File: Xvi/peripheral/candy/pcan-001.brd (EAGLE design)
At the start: 72 x 72 mm, 24 parts

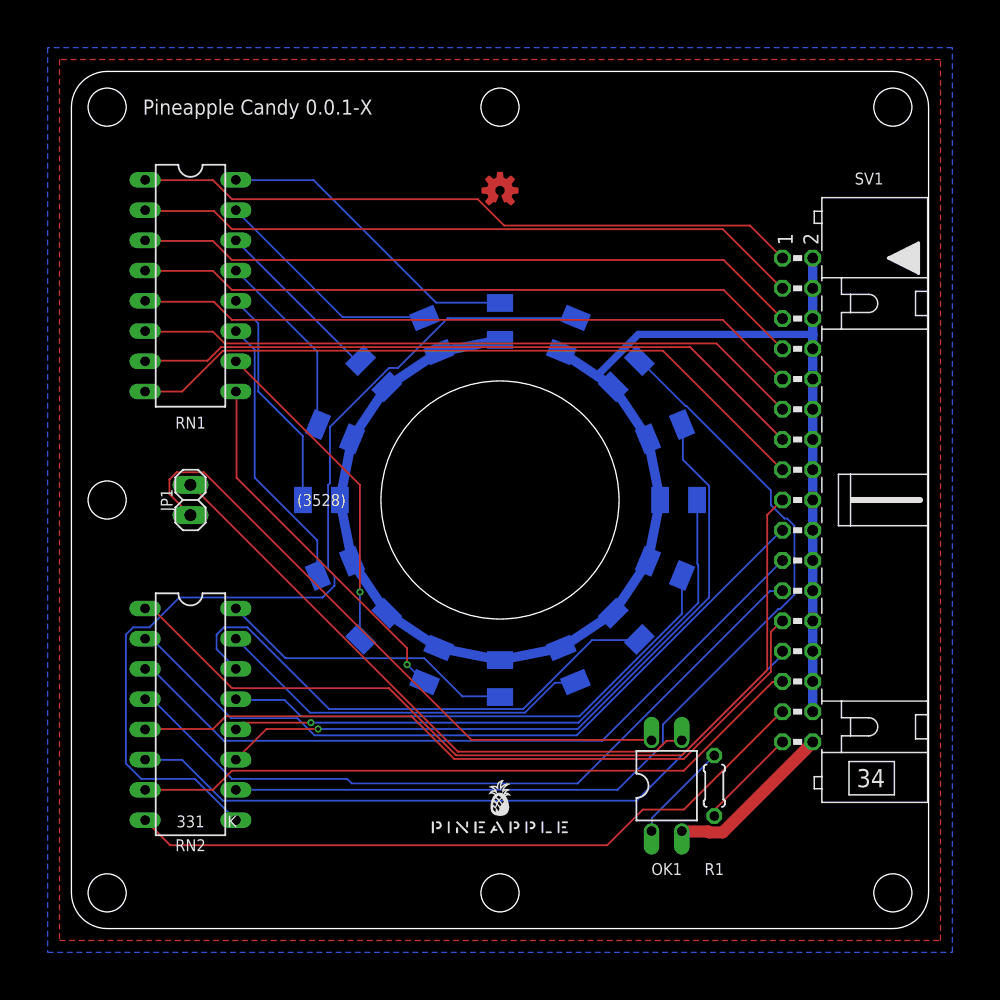
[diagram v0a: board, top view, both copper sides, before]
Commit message: Dual LEDs.
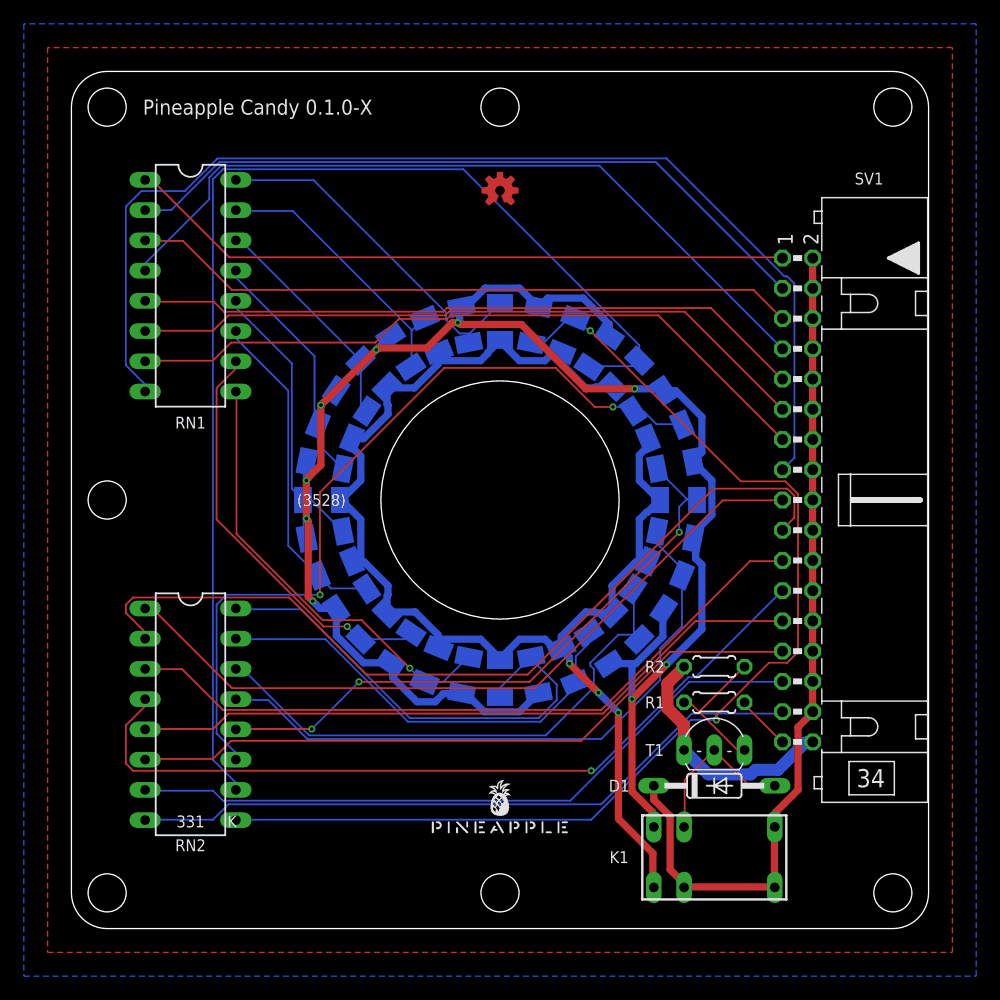
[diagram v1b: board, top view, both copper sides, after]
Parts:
- removed JP1: Optorelay, pinhead:1X02
- removed OK1: LTV816, optocoupler:DIL04
- added D1: 1N4446, diode:DO35-10
- added K1: G5V1, relay:G5V1
- added L17, L18, L19, L20, L21, L22, L23, L24, L25, L26, L27, L28, L29, L30, L31, L32: LP-T35XW-80-BJ, led:KA-3528ASYC
- added R2: (no value), rcl:0204/5
- added T1: 2SC1815, transistor:TO92-ECB
- R1: value 220 -> (none)
- moved R1 7.00 mm to (54.0, 19.0), turned to 0 degrees
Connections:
- removed net N$1: L01.C, RN1.16
- removed net N$10: L10.C, RN2.15
- removed net N$11: L11.C, RN2.14
- removed net N$12: L12.C, RN2.13
- removed net N$13: L13.C, RN2.12
- removed net N$14: L14.C, RN2.11
- removed net N$15: L15.C, RN2.10
- removed net N$16: L16.C, RN2.9
- removed net N$2: L02.C, RN1.15
- removed net N$20: JP1.1, OK1.4
- removed net N$3: L03.C, RN1.14
- removed net N$4: L04.C, RN1.13
- removed net N$5: L05.C, RN1.12
- removed net N$6: L06.C, RN1.11
- removed net N$7: L07.C, RN1.10
- removed net N$8: L08.C, RN1.9
- removed net N$9: L09.C, RN2.16
- new net LD00K: L01.C, L17.C, RN1.16
- new net LD01K: L02.C, L18.C, RN1.15
- new net LD02K: L03.C, L19.C, RN1.14
- new net LD03K: L04.C, L20.C, RN1.13
- new net LD04K: L05.C, L21.C, RN1.12
- new net LD05K: L06.C, L22.C, RN1.11
- new net LD06K: L07.C, L23.C, RN1.10
- new net LD07K: L08.C, L24.C, RN1.9
- new net LD08K: L09.C, L25.C, RN2.16
- new net LD09K: L10.C, L26.C, RN2.15
- new net LD10K: L11.C, L27.C, RN2.14
- new net LD11K: L12.C, L28.C, RN2.13
- new net LD12K: L13.C, L29.C, RN2.12
- new net LD13K: L14.C, L30.C, RN2.11
- new net LD14K: L15.C, L31.C, RN2.10
- new net LD15K: L16.C, L32.C, RN2.9
- new net VINA: K1.1, L01.A, L02.A, L03.A, L04.A, L05.A, L06.A, L07.A, L08.A, L09.A, L10.A, L11.A, L12.A, L13.A, L14.A, L15.A, L16.A
- new net VINB: K1.10, L17.A, L18.A, L19.A, L20.A, L21.A, L22.A, L23.A, L24.A, L25.A, L26.A, L27.A, L28.A, L29.A, L30.A, L31.A, L32.A
- net GND: now also R2.1, T1.E; no longer OK1.2
- net MNTR: now also R1.2; no longer R1.1
- net N$17: now also D1.A, K1.9, T1.C; no longer OK1.1, R1.2
- net N$19: now also R1.1, R2.2, T1.B; no longer JP1.2, OK1.3
- net VIN: now also D1.C, K1.2, K1.5, K1.6; no longer L01.A, L02.A, L03.A, L04.A, L05.A, L06.A, L07.A, L08.A, L09.A, L10.A, L11.A, L12.A, L13.A, L14.A, L15.A, L16.A
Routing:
- net VINB: track 0.00 -> 155.4 mm, vias 0 -> 9
- net VINA: track 0.00 -> 117.9 mm, vias 0 -> 3
- net LD14K: track 0.00 -> 100.1 mm
- net LD15K: track 0.00 -> 96.0 mm, vias 0 -> 2
- net N$15: track 80.0 -> 0.00 mm
- net N$16: track 79.3 -> 0.00 mm
- net LD13K: track 0.00 -> 68.1 mm, vias 0 -> 2
- net VIN: track 136.4 -> 71.5 mm
- net N$14: track 60.9 -> 0.00 mm, vias 1 -> 0
- net N$20: track 53.8 -> 0.00 mm
- net LD11K: track 0.00 -> 53.2 mm
- net N$13: track 51.9 -> 0.00 mm, vias 1 -> 0
- net LD12K: track 0.00 -> 51.6 mm, vias 0 -> 3
- net LD10K: track 0.00 -> 46.0 mm
- net N$12: track 44.9 -> 0.00 mm
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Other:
- board text added: "Pineapple Candy 0.1.0-X"
- board text removed: "Pineapple Candy 0.0.1-X"
